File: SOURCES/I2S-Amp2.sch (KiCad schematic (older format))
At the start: 49 parts, among them P1 CONN_02X08, P2 CONN_01X02, P3 CONN_01X02, P4 CONN_01X02, U1 SN74LVC14ADG4, U2 LM317_SOT223, U3 TAS5760MDCAR

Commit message: adding AMPx2 done
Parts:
- removed P1: CONN_02X08, Connect:IDC_Header_Straight_16pins, symbol CONN_02X08
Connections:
- net labels added: MCLK2, MP10, MP11, MP7
- wire segments 160 -> 147
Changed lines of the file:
@@
 $Descr A4 11693 8268
 encoding utf-8
-Sheet 2 6
+Sheet 7 7
 Title ""
 Date ""
@@
 $EndComp
 $Comp
-L CONN_02X08 P1
-U 1 1 5752C822
-P 4650 4450
-F 0 "P1" H 4650 4900 50  0000 C CNN
-F 1 "CONN_02X08" V 4650 4450 50  0000 C CNN
-F 2 "Connect:IDC_Header_Straight_16pins" H 4650 3250 50  0001 C CNN
-F 3 "http://www.mouser.com/ds/2/445/6120xx21621-265830.pdf" H 4650 3250 50  0001 C CNN
-F 4 "61201621621" H 4650 4450 60  0001 C CNN "Mfr.Nr."
-	1    4650 4450
-	1    0    0    -1
-$EndComp
-$Comp
 L R R6
 U 1 1 5752F884
@@
 F 4 "CRCW0603100KFKEA" V 1850 2850 60  0001 C CNN "Mfr.Nr."
 	1    1850 2850
-	1    0    0    -1
-$EndComp
-$Comp
-L GND #PWR030
-U 1 1 575366A3
-P 4950 4900
-F 0 "#PWR030" H 4950 4650 50  0001 C CNN
-F 1 "GND" H 4950 4750 50  0000 C CNN
-F 2 "" H 4950 4900 50  0000 C CNN
-F 3 "" H 4950 4900 50  0000 C CNN
-	1    4950 4900
 	1    0    0    -1
 $EndComp
@@
 	10600 3650 10600 3450
 Wire Wire Line
-	4050 4800 4400 4800
-Wire Wire Line
-	4150 4400 4400 4400
-Wire Wire Line
-	4250 4300 4400 4300
-Wire Wire Line
-	4350 4500 4400 4500
-Wire Wire Line
-	4900 4100 4950 4100
-Wire Wire Line
-	4950 4100 4950 4900
-Wire Wire Line
-	4900 4200 4950 4200
-Connection ~ 4950 4200
-Wire Wire Line
-	4900 4300 4950 4300
-Connection ~ 4950 4300
-Wire Wire Line
-	4900 4400 4950 4400
-Connection ~ 4950 4400
-Wire Wire Line
-	4900 4500 4950 4500
-Connection ~ 4950 4500
-Wire Wire Line
-	4900 4600 4950 4600
-Connection ~ 4950 4600
-Wire Wire Line
-	4900 4700 4950 4700
-Connection ~ 4950 4700
-Wire Wire Line
-	4900 4800 4950 4800
-Connection ~ 4950 4800
-Wire Wire Line
 	4450 5320 4450 5700
 Connection ~ 7600 1800
@@
 Wire Wire Line
 	4350 3400 4350 3550
-Wire Wire Line
-	4350 3950 4350 4500
-Wire Wire Line
-	4250 3950 4250 4300
-Wire Wire Line
-	4150 3950 4150 4400
-Wire Wire Line
-	4050 3950 4050 4800
 $Comp
 L FILTER FB1
@@
 	1    0    0    -1
 $EndComp
+$Comp
+L +3V3 #PWR?
+U 1 1 5B04DB98
+P 3350 2550
+F 0 "#PWR?" H 3350 2400 50  0001 C CNN
+F 1 "+3V3" H 3350 2690 50  0000 C CNN
+F 2 "" H 3350 2550 60  0000 C CNN
+F 3 "" H 3350 2550 60  0000 C CNN
+	1    3350 2550
+	0    1    1    0
+$EndComp
+$Comp
+L +3V3 #PWR?
+U 1 1 5B0433C1
+P 3750 2600
+F 0 "#PWR?" H 3750 2450 50  0001 C CNN
+F 1 "+3V3" H 3750 2740 50  0000 C CNN
+F 2 "" H 3750 2600 60  0000 C CNN
+F 3 "" H 3750 2600 60  0000 C CNN
+	1    3750 2600
+	1    0    0    -1
+$EndComp
+Text GLabel 4350 4030 3    44   Input ~ 0
+MP10
+Text GLabel 4250 4030 3    44   Input ~ 0
+MP7
+Text GLabel 4150 4030 3    44   Input ~ 0
+MP11
+Text GLabel 4050 4030 3    44   Input ~ 0
+MCLK2
+Wire Wire Line
+	4050 4030 4050 3950
+Wire Wire Line
+	4150 3950 4150 4030
+Wire Wire Line
+	4250 3950 4250 4030
+Wire Wire Line
+	4350 3950 4350 4030
 $EndSCHEMATC

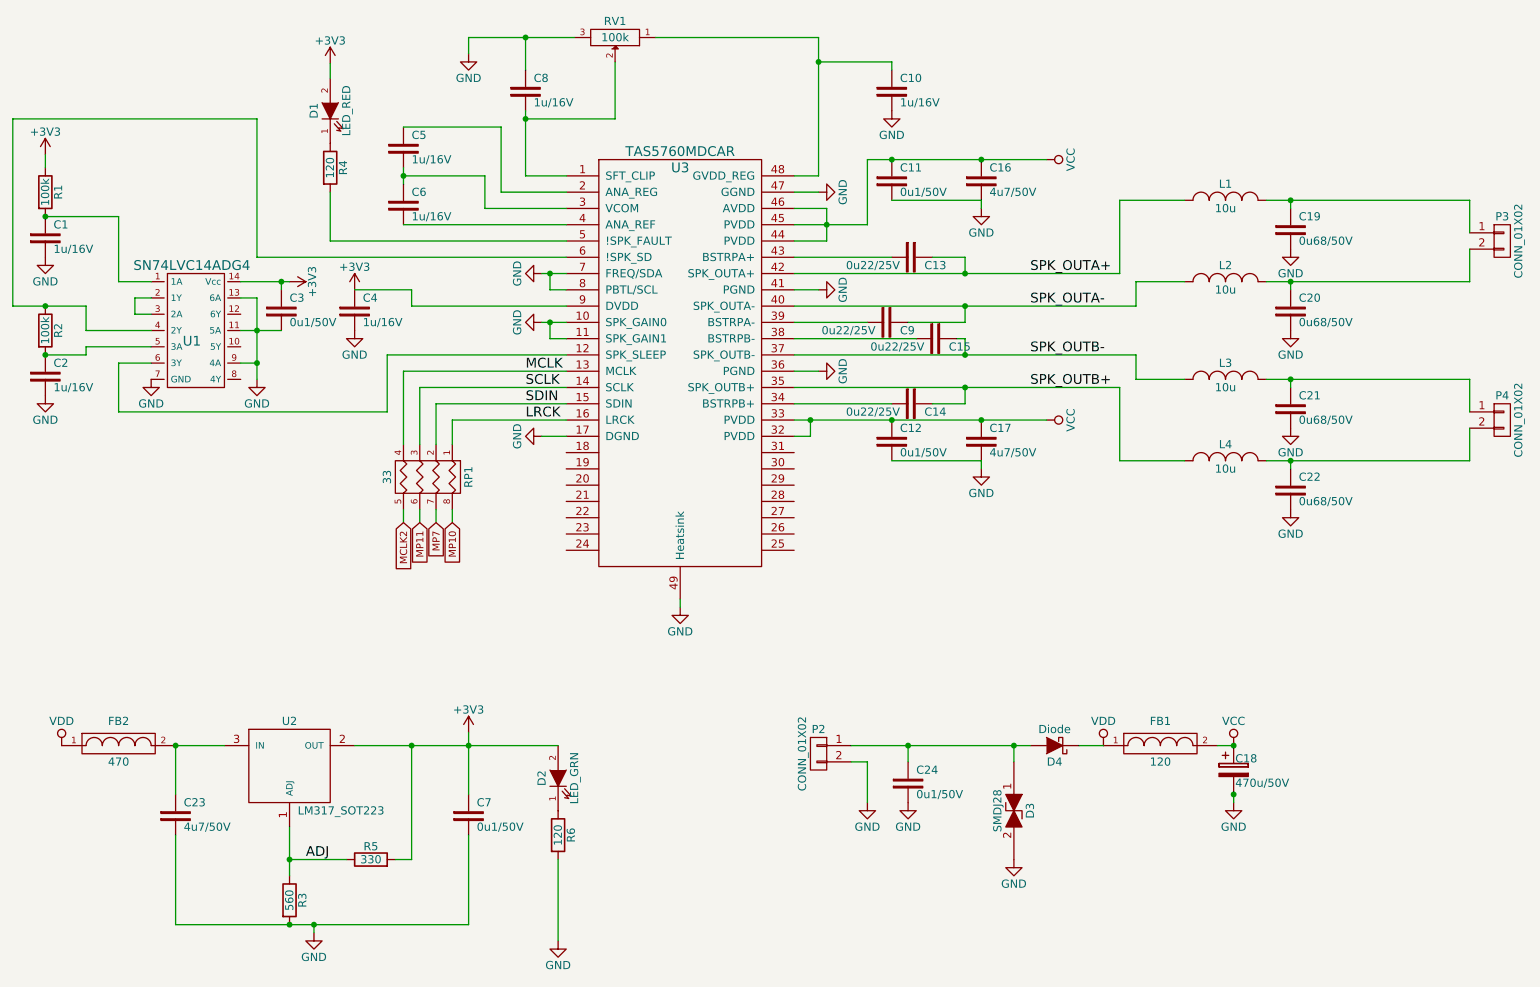
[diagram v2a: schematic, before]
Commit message: added analog input
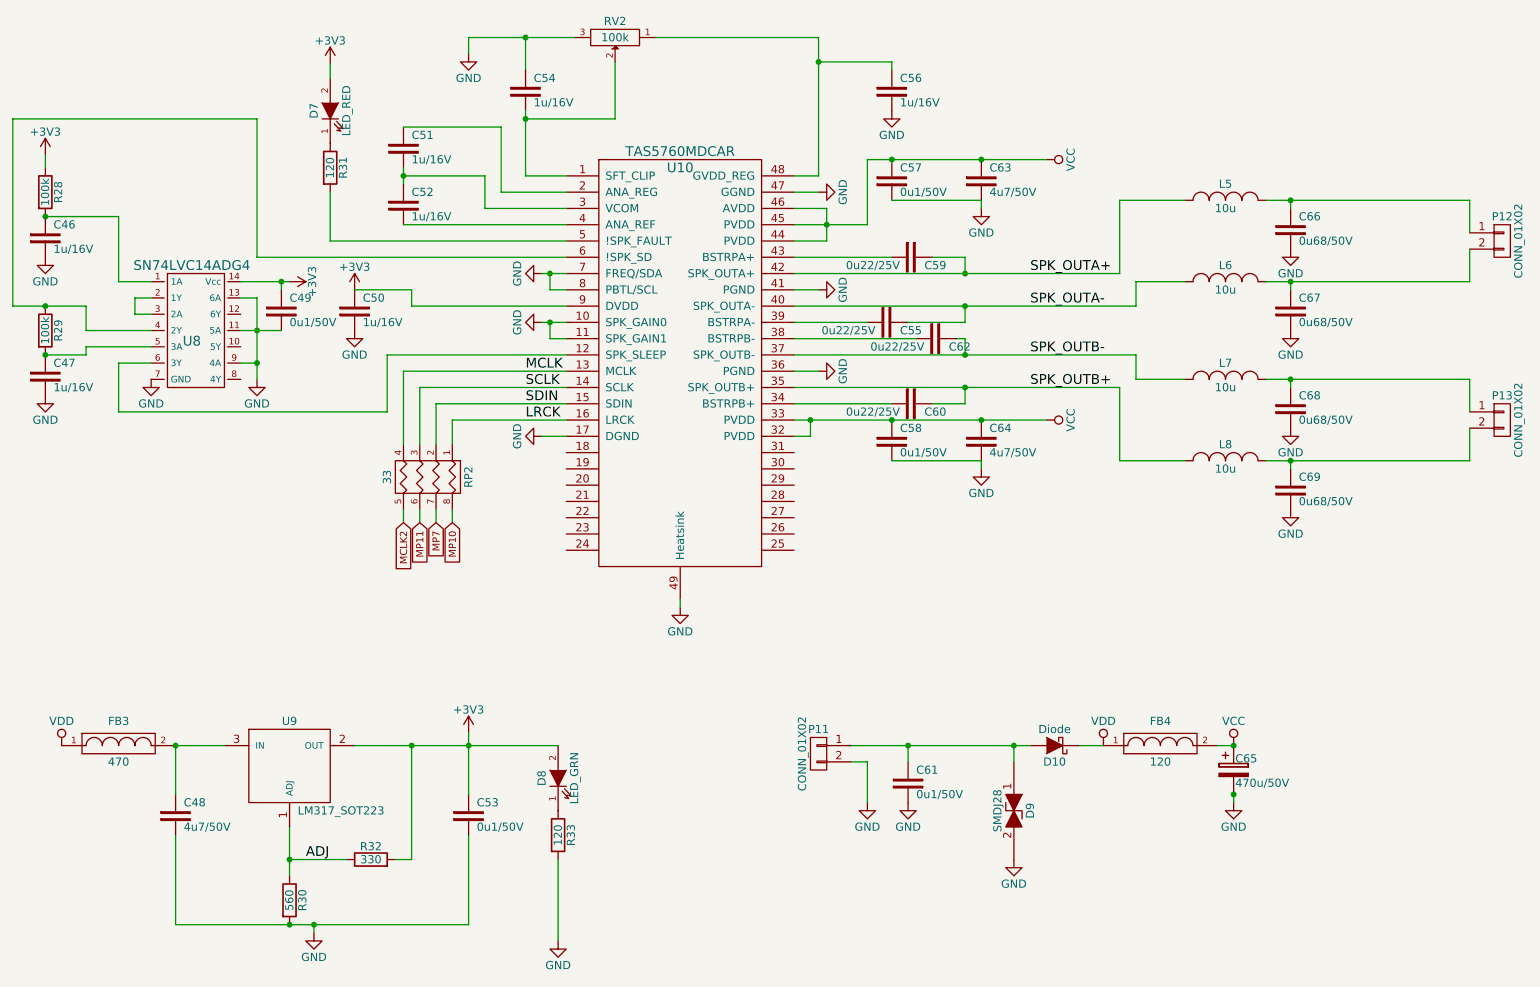
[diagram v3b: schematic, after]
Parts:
- removed C1, C10, C8: 1u/16V, Capacitors_SMD:C_0603, symbol Capacitor
- removed C11, C12, C3, C7: 0u1/50V, Capacitors_SMD:C_0603, symbol Capacitor
- removed C17: 4u7/50V, Capacitors_SMD:C_1206, symbol Capacitor
- removed C19, C21: 0u68/50V, Capacitors_SMD:C_1206, symbol Capacitor
- removed P4: CONN_01X02, MyFootprints:Connector0.5, symbol CONN_01X02
- removed R3: 560, Resistors_SMD:R_0603, symbol R
- removed R4, R6: 120, Resistors_SMD:R_0603, symbol R
- removed R5: 330, Resistors_SMD:R_0603, symbol R
- removed RP1: 33, Resistors_SMD:R_Array_Concave_4x0603, symbol R_PACK4
- removed RV1: 100k, MyFootprints:M64Z104KB40, symbol POT
- removed U2: LM317_SOT223, TO_SOT_Packages_SMD:SOT-223, symbol LM317_SOT223
- removed U3: TAS5760MDCAR, MyFootprints:HTSSOP-48, symbol TAS5760MDCAR
- added C46, C54, C56: 1u/16V, Capacitors_SMD:C_0603, symbol Capacitor
- added C49, C53, C57, C58: 0u1/50V, Capacitors_SMD:C_0603, symbol Capacitor
- added C64: 4u7/50V, Capacitors_SMD:C_1206, symbol Capacitor
- added C66, C68: 0u68/50V, Capacitors_SMD:C_1206, symbol Capacitor
- added P13: CONN_01X02, MyFootprints:Connector0.5, symbol CONN_01X02
- added R30: 560, Resistors_SMD:R_0603, symbol R
- added R31, R33: 120, Resistors_SMD:R_0603, symbol R
- added R32: 330, Resistors_SMD:R_0603, symbol R
- added RP2: 33, Resistors_SMD:R_Array_Concave_4x0603, symbol R_PACK4
- added RV2: 100k, MyFootprints:M64Z104KB40, symbol POT
- added U10: TAS5760MDCAR, MyFootprints:HTSSOP-48, symbol TAS5760MDCAR
- added U9: LM317_SOT223, TO_SOT_Packages_SMD:SOT-223, symbol LM317_SOT223
- renumbered C2 to C47, C23 to C48, C4 to C50, C5 to C51, C6 to C52, C9 to C55, C13 to C59, C14 to C60, C24 to C61, C15 to C62, C16 to C63, C18 to C65, C20 to C67, C22 to C69, D4 to D10, D1 to D7, D2 to D8, D3 to D9, FB2 to FB3, FB1 to FB4, L1 to L5, L2 to L6, L3 to L7, L4 to L8, P2 to P11, P3 to P12, R1 to R28, R2 to R29, U1 to U8
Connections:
- net +3V3: now also C49.1, C53.1, R32.2, U10.9 (DVDD), U9.2 (OUT), U9.4
- net ADJ: now also R30.1, R32.1, U9.1 (ADJ)
- net GND: now also C46.2, C49.2, C53.2, C54.1, C56.2, C57.2, C58.2, C64.2, C66.2, C68.2, R30.2, R33.2, RV2.3, U10.10 (SPK_GAIN0), U10.11 (SPK_GAIN1), U10.17 (DGND), U10.36 (PGND), U10.41 (PGND), U10.47 (GGND), U10.49 (Heatsink), U10.7 (FREQ/SDA), U10.8 (PBTL/SCL)
- net LRCK: now also RP2.1 (P1), U10.16 (LRCK)
- net MCLK: now also RP2.4 (P4), U10.13 (MCLK)
- net MCLK2: now also RP2.5 (R4)
- net MP10: now also RP2.8 (R1)
- net MP11: now also RP2.6 (R3)
- net MP7: now also RP2.7 (R2)
- net SCLK: now also RP2.3 (P3), U10.14 (SCLK)
- net SDIN: now also RP2.2 (P2), U10.15 (SDIN)
- net SPK_OUTA+: now also U10.42 (SPK_OUTA+)
- net SPK_OUTA-: now also U10.40 (SPK_OUTA-)
- net SPK_OUTB+: now also U10.35 (SPK_OUTB+)
- net SPK_OUTB-: now also U10.37 (SPK_OUTB-)
- net VCC: now also C57.1, C58.1, C64.1, U10.32 (PVDD), U10.33 (PVDD), U10.44 (PVDD), U10.45 (PVDD), U10.46 (AVDD)
- net at U8.6 (3Y): now also U10.12 (SPK_SLEEP)
- net at C51.1: now also U10.2 (ANA_REG)
- net at C51.2, C52.1: now also U10.3 (VCOM)
- net at C60.2: now also U10.34 (BSTRPB+)
- net at C62.2: now also U10.38 (BSTRPB-)
- net at C55.2: now also U10.39 (BSTRPA-)
- net at C52.2: now also U10.4 (ANA_REF)
- net at C59.2: now also U10.43 (BSTRPA+)
- net at R29.1, U8.4 (2Y): now also U10.6 (!SPK_SD)
- net at L5.2, P12.1 (P1): now also C66.1
- net at L7.2: now also C68.1, P13.1 (P1)
- net at C69.1, L8.2: now also P13.2 (P2)
- net at C48.1, FB3.2: now also U9.3 (IN)
- net at D7.1 (K): now also R31.1
- net at R28.2, U8.1 (1A): now also C46.1
- net at D8.1 (K): now also R33.1
- new net: C54.2, RV2.2, U10.1 (SFT_CLIP)
- new net: U10.31, U10.~
- new net: C56.1, RV2.1, U10.48 (GVDD_REG)
- new net: R31.2, U10.5 (!SPK_FAULT)

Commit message: added power
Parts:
- C49, C57, C58: value 0u1/50V -> 0u1/35V
- C63, C64: value 4u7/50V -> 4u7/35V
- C66, C67, C68, C69: value 0u68/50V -> 0u68/35V
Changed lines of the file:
@@
 P 7600 1950
 F 0 "C63" H 7650 2050 50  0000 L CNN
-F 1 "4u7/50V" H 7650 1900 50  0000 L CNN
+F 1 "4u7/35V" H 7650 1900 50  0000 L CNN
 F 2 "Capacitors_SMD:C_1206" V 7300 2090 50  0001 C CNN
 F 3 "http://www.murata.com/products/catalog/pdf/c02e.pdf" V 7300 2090 50  0001 C CNN
@@
 P 7050 1950
 F 0 "C57" H 7100 2050 50  0000 L CNN
-F 1 "0u1/50V" H 7100 1900 50  0000 L CNN
+F 1 "0u1/35V" H 7100 1900 50  0000 L CNN
 F 2 "Capacitors_SMD:C_0603" V 6750 2090 50  0001 C CNN
 F 3 "http://www.murata.com/products/catalog/pdf/c02e.pdf" V 6750 2090 50  0001 C CNN
@@
 P 7600 3550
 F 0 "C64" H 7650 3650 50  0000 L CNN
-F 1 "4u7/50V" H 7650 3500 50  0000 L CNN
+F 1 "4u7/35V" H 7650 3500 50  0000 L CNN
 F 2 "Capacitors_SMD:C_1206" V 7300 3690 50  0001 C CNN
 F 3 "http://www.murata.com/products/catalog/pdf/c02e.pdf" V 7300 3690 50  0001 C CNN
@@
 P 7050 3550
 F 0 "C58" H 7100 3650 50  0000 L CNN
-F 1 "0u1/50V" H 7100 3500 50  0000 L CNN
+F 1 "0u1/35V" H 7100 3500 50  0000 L CNN
 F 2 "Capacitors_SMD:C_0603" V 6750 3690 50  0001 C CNN
 F 3 "http://www.murata.com/products/catalog/pdf/c02e.pdf" V 6750 3690 50  0001 C CNN
@@
 P 9500 2250
 F 0 "C66" H 9550 2350 50  0000 L CNN
-F 1 "0u68/50V" H 9550 2200 50  0000 L CNN
+F 1 "0u68/35V" H 9550 2200 50  0000 L CNN
 F 2 "Capacitors_SMD:C_1206" V 9200 2390 50  0001 C CNN
 F 3 "http://www.murata.com/products/catalog/pdf/c03e.pdf" V 9200 2390 50  0001 C CNN
@@
 P 9500 2750
 F 0 "C67" H 9550 2850 50  0000 L CNN
-F 1 "0u68/50V" H 9550 2700 50  0000 L CNN
+F 1 "0u68/35V" H 9550 2700 50  0000 L CNN
 F 2 "Capacitors_SMD:C_1206" V 9200 2890 50  0001 C CNN
 F 3 "http://www.murata.com/products/catalog/pdf/c03e.pdf" V 9200 2890 50  0001 C CNN
@@
 P 9500 3350
 F 0 "C68" H 9550 3450 50  0000 L CNN
-F 1 "0u68/50V" H 9550 3300 50  0000 L CNN
+F 1 "0u68/35V" H 9550 3300 50  0000 L CNN
 F 2 "Capacitors_SMD:C_1206" V 9200 3490 50  0001 C CNN
 F 3 "http://www.murata.com/products/catalog/pdf/c03e.pdf" V 9200 3490 50  0001 C CNN
@@
 P 9500 3850
 F 0 "C69" H 9550 3950 50  0000 L CNN
-F 1 "0u68/50V" H 9550 3800 50  0000 L CNN
+F 1 "0u68/35V" H 9550 3800 50  0000 L CNN
 F 2 "Capacitors_SMD:C_1206" V 9200 3990 50  0001 C CNN
 F 3 "http://www.murata.com/products/catalog/pdf/c03e.pdf" V 9200 3990 50  0001 C CNN
@@
 P 3300 2750
 F 0 "C49" H 3350 2850 50  0000 L CNN
-F 1 "0u1/50V" H 3350 2700 50  0000 L CNN
+F 1 "0u1/35V" H 3350 2700 50  0000 L CNN
 F 2 "Capacitors_SMD:C_0603" V 3000 2890 50  0001 C CNN
 F 3 "http://www.murata.com/products/catalog/pdf/c02e.pdf" V 3000 2890 50  0001 C CNN

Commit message: modifications amp
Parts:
- removed C48: 4u7/50V, Capacitors_SMD:C_1206, symbol Capacitor
- removed C53, C61: 0u1/50V, Capacitors_SMD:C_0603, symbol Capacitor
- removed C65: 470u/50V, Capacitors_ThroughHole:C_Radial_D10_L16_P5, symbol CP
- removed D10: Diode, MyFootprints:PowerDI5, symbol D_Schottky
- removed D8: LED_GRN, LEDs:LED_0603, symbol LED
- removed D9: SMDJ28, Diodes_SMD:DO-214AB, symbol TVS
- removed FB3: 470, Capacitors_SMD:C_0603, symbol FILTER
- removed FB4: 120, Capacitors_SMD:C_1206, symbol FILTER
- removed P11: CONN_01X02, MyFootprints:Connector0.5, symbol CONN_01X02
- removed R30: 560, Resistors_SMD:R_0603, symbol R
- removed R32: 330, Resistors_SMD:R_0603, symbol R
- removed R33: 120, Resistors_SMD:R_0603, symbol R
- removed RP2: 33, Resistors_SMD:R_Array_Concave_4x0603, symbol R_PACK4
- removed U9: LM317_SOT223, TO_SOT_Packages_SMD:SOT-223, symbol LM317_SOT223
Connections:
- net LRCK is gone; now on net MP10: U10.16 (LRCK)
- net MCLK is gone; now on net MCLK2: U10.13 (MCLK)
- net SCLK is gone; now on net MP11: U10.14 (SCLK)
- net SDIN is gone; now on net MP7: U10.15 (SDIN)

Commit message: design rule check
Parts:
- renumbered C46 to C69, C47 to C70, C49 to C71, C50 to C72, C51 to C73, C52 to C74, C54 to C75, C55 to C76, C56 to C77, C57 to C78, C58 to C79, C59 to C80, C60 to C81, C62 to C82, C63 to C83, C64 to C84, C66 to C85, C67 to C86, C68 to C87, C69 to C88, D7 to D9, L5 to L6, L6 to L7, L7 to L8, L8 to L9, P12 to P14, P13 to P15, R28 to R37, R29 to R38, R31 to R39, U10 to U9
